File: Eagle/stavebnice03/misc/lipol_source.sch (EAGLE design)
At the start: 27 parts

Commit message: layer coloring and place drawing moved to docu layer + changed sizes of names and values
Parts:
- removed LED2: (no value), led:LED3MM
- removed U$10: JUMPER5M, !stavebnice03:JUMPER5M
- added D1: LED1.8, !stavebnice03:LED1.8
- added PROG: JUMPER5M, !stavebnice03:JUMPER5M
- C7: value 4,7uF -> 4.7uF
- R5: value 10k -> 100k
- T1: value P-MOSFET-FDV304P -> FDV304P
- renumbered NC7SB3157P6X(1) to U3, NC7SB3157P6X(2) to U2, U$1 to U1, U$2 to USB, U$5 to OUT, U$9 to T1
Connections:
- net GND: now also PROG.3, USB.NC; no longer U$10.3
- net N$14: now also PROG.1; no longer U$10.5
- net N$15: now also D1.K; no longer LED2.C
- net N$16: now also D1.A; no longer LED2.A
- net N$4: now also PROG.4; no longer U$10.2
- net N$7: now also PROG.5; no longer U$10.1
- net VCC: now also PROG.2; no longer U$10.4

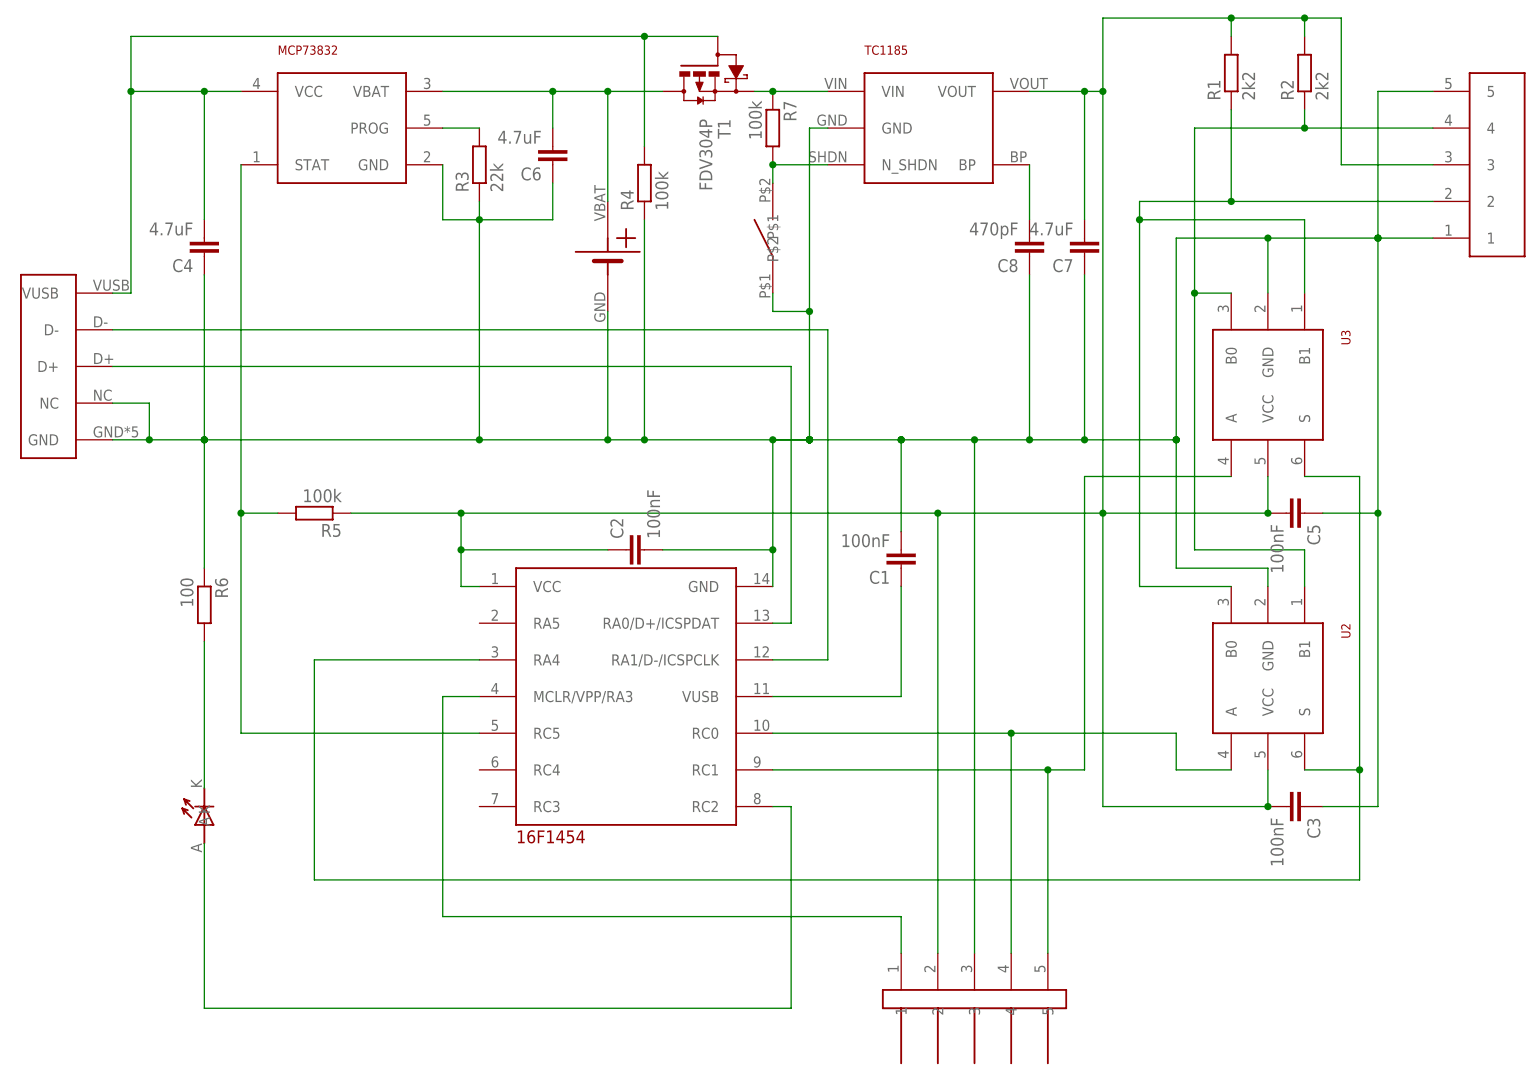
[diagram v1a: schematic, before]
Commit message: added bootloder touch point and pull up resistor to switcher + increased interface led resistor, it lighted too much
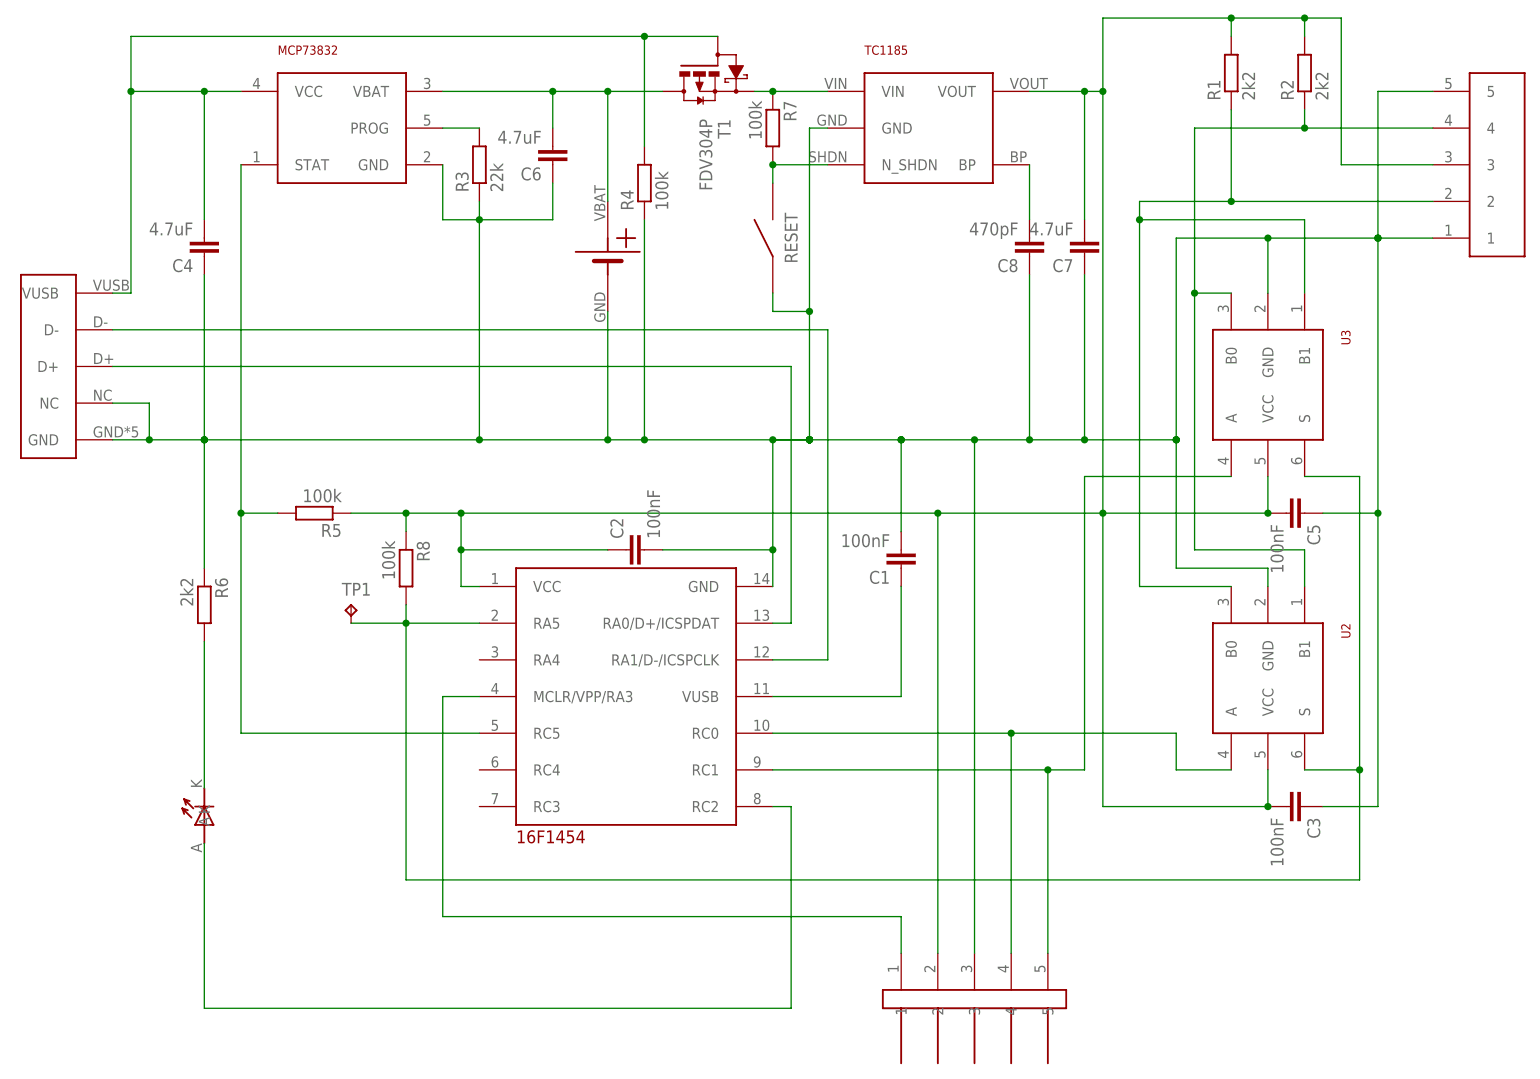
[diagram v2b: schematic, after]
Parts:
- added R8: 100k, resistor:R-EU_R0603
- added TP1: TPB1,27, testpad:TPB1,27
- R6: value 100 -> 2k2
- renumbered U$6 to RESET
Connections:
- net N$1: now also R8.2, TP1.TP, U1.RA5; no longer U1.RA4
- net VCC: now also R8.1
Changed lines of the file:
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@@
 <classes>
 <class number="0" name="default" width="0" drill="0">
+<clearance class="0" value="0.205"/>
 </class>
 </classes>
@@
 <part name="PROG" library="!stavebnice03" deviceset="JUMPER5M" device=""/>
 <part name="R5" library="resistor" deviceset="R-EU_" device="R0603" value="100k"/>
-<part name="R6" library="resistor" deviceset="R-EU_" device="R0603" value="100"/>
+<part name="R6" library="resistor" deviceset="R-EU_" device="R0603" value="2k2"/>
 <part name="C8" library="resistor" deviceset="C-EU" device="C0603K" value="470pF"/>
 <part name="R7" library="resistor" deviceset="R-EU_" device="R0603" value="100k"/>
-<part name="U$6" library="!stavebnice03" deviceset="BYTTON-B3U" device=""/>
+<part name="RESET" library="!stavebnice03" deviceset="BYTTON-B3U" device=""/>
 <part name="D1" library="!stavebnice03" deviceset="LED1.8" device=""/>
+<part name="R8" library="resistor" deviceset="R-EU_" device="R0603" value="100k"/>
+<part name="TP1" library="testpad" deviceset="TP" device="B1,27"/>
 </parts>
 <sheets>
@@
 <instance part="C8" gate="G$1" x="200.66" y="144.78" rot="R180"/>
 <instance part="R7" gate="G$1" x="165.1" y="162.56" rot="R270"/>
-<instance part="U$6" gate="G$1" x="165.1" y="147.32" rot="R90"/>
+<instance part="RESET" gate="G$1" x="165.1" y="147.32" rot="R90"/>
 <instance part="D1" gate="G$1" x="86.36" y="66.04" rot="R90"/>
+<instance part="R8" gate="G$1" x="114.3" y="101.6" rot="R270"/>
+<instance part="TP1" gate="G$1" x="106.68" y="96.52"/>
 </instances>
 <busses>
@@
 <wire x1="170.18" y1="137.16" x2="170.18" y2="119.38" width="0.1524" layer="91"/>
 <junction x="170.18" y="137.16"/>
-<pinref part="U$6" gate="G$1" pin="P$1"/>
+<pinref part="RESET" gate="G$1" pin="P$1"/>
 <wire x1="165.1" y1="139.7" x2="165.1" y2="137.16" width="0.1524" layer="91"/>
 <wire x1="165.1" y1="137.16" x2="170.18" y2="137.16" width="0.1524" layer="91"/>
@@
 <junction x="187.96" y="109.22"/>
 <pinref part="R5" gate="G$1" pin="1"/>
-<wire x1="106.68" y1="109.22" x2="121.92" y2="109.22" width="0.1524" layer="91"/>
+<wire x1="106.68" y1="109.22" x2="114.3" y2="109.22" width="0.1524" layer="91"/>
 <junction x="121.92" y="109.22"/>
 <pinref part="PROG" gate="G$1" pin="2"/>
+<pinref part="R8" gate="G$1" pin="1"/>
+<wire x1="114.3" y1="109.22" x2="121.92" y2="109.22" width="0.1524" layer="91"/>
+<wire x1="114.3" y1="106.68" x2="114.3" y2="109.22" width="0.1524" layer="91"/>
+<junction x="114.3" y="109.22"/>
 </segment>
 </net>
@@
 <segment>
 <wire x1="246.38" y1="73.66" x2="246.38" y2="58.42" width="0.1524" layer="91"/>
-<wire x1="246.38" y1="58.42" x2="101.6" y2="58.42" width="0.1524" layer="91"/>
-<wire x1="101.6" y1="58.42" x2="101.6" y2="88.9" width="0.1524" layer="91"/>
-<pinref part="U1" gate="G$1" pin="RA4"/>
-<wire x1="101.6" y1="88.9" x2="124.46" y2="88.9" width="0.1524" layer="91"/>
+<wire x1="246.38" y1="58.42" x2="114.3" y2="58.42" width="0.1524" layer="91"/>
+<wire x1="114.3" y1="58.42" x2="114.3" y2="93.98" width="0.1524" layer="91"/>
 <pinref part="U2" gate="G$1" pin="S"/>
 <wire x1="238.76" y1="73.66" x2="246.38" y2="73.66" width="0.1524" layer="91"/>
@@
 <wire x1="246.38" y1="114.3" x2="238.76" y2="114.3" width="0.1524" layer="91"/>
 <junction x="246.38" y="73.66"/>
+<pinref part="U1" gate="G$1" pin="RA5"/>
+<wire x1="114.3" y1="93.98" x2="124.46" y2="93.98" width="0.1524" layer="91"/>
+<pinref part="R8" gate="G$1" pin="2"/>
+<wire x1="114.3" y1="93.98" x2="114.3" y2="96.52" width="0.1524" layer="91"/>
+<junction x="114.3" y="93.98"/>
+<pinref part="TP1" gate="G$1" pin="TP"/>
+<wire x1="106.68" y1="93.98" x2="114.3" y2="93.98" width="0.1524" layer="91"/>
 </segment>
 </net>
@@
 <pinref part="R7" gate="G$1" pin="2"/>
 <junction x="165.1" y="157.48"/>
-<pinref part="U$6" gate="G$1" pin="P$2"/>
+<pinref part="RESET" gate="G$1" pin="P$2"/>
 <wire x1="165.1" y1="157.48" x2="165.1" y2="154.94" width="0.1524" layer="91"/>
 </segment>

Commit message: eagle adjustment for the Jíťa version
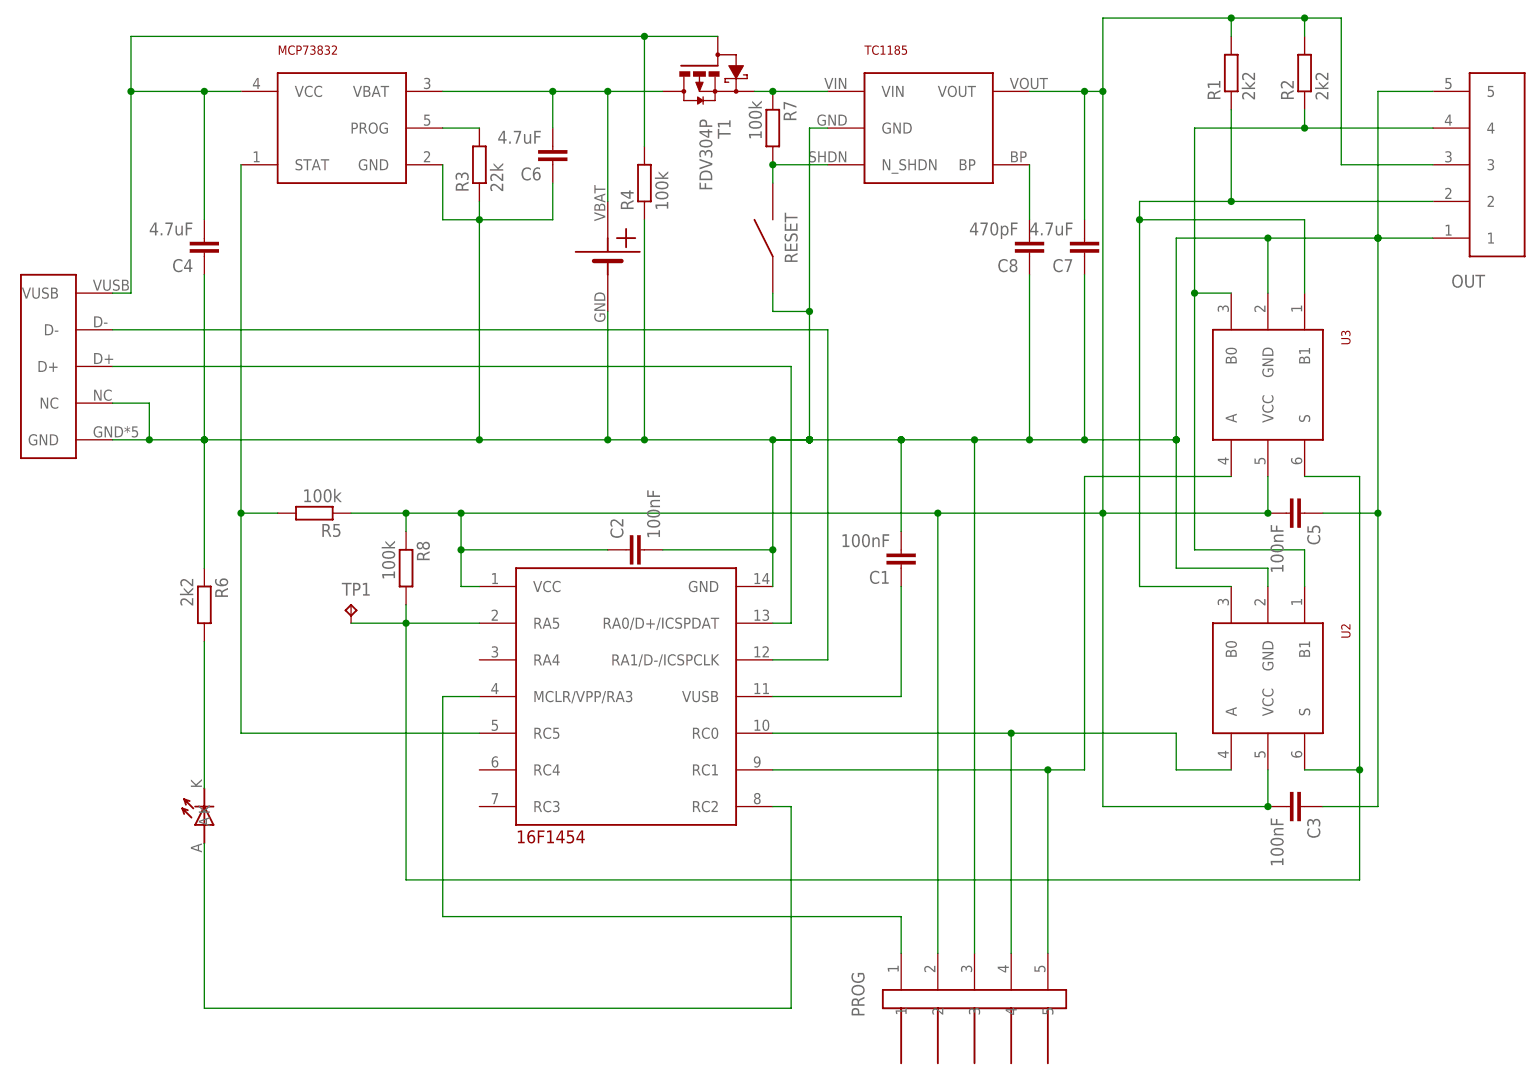
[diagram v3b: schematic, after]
